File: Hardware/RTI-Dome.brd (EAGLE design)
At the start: 80 x 71.1 mm, 50 parts, among them IC1 24AA128ST, IC2 74LVC244, IC3 FT232RL, IC4 74ABT244, X13 PN61729-S

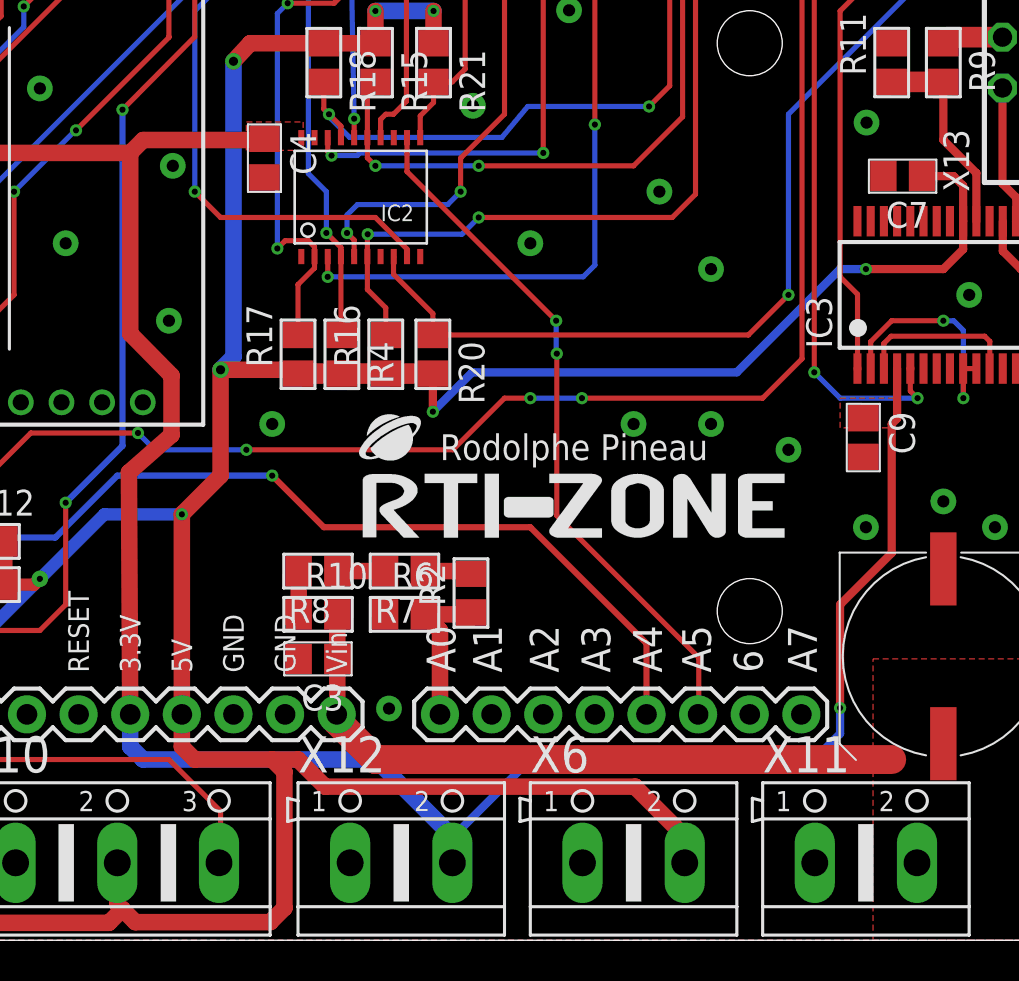
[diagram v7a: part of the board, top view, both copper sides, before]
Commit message: Some routing optimisation. Remove 3.3V header as it's not needed anymore. Added 2 ground for good measure
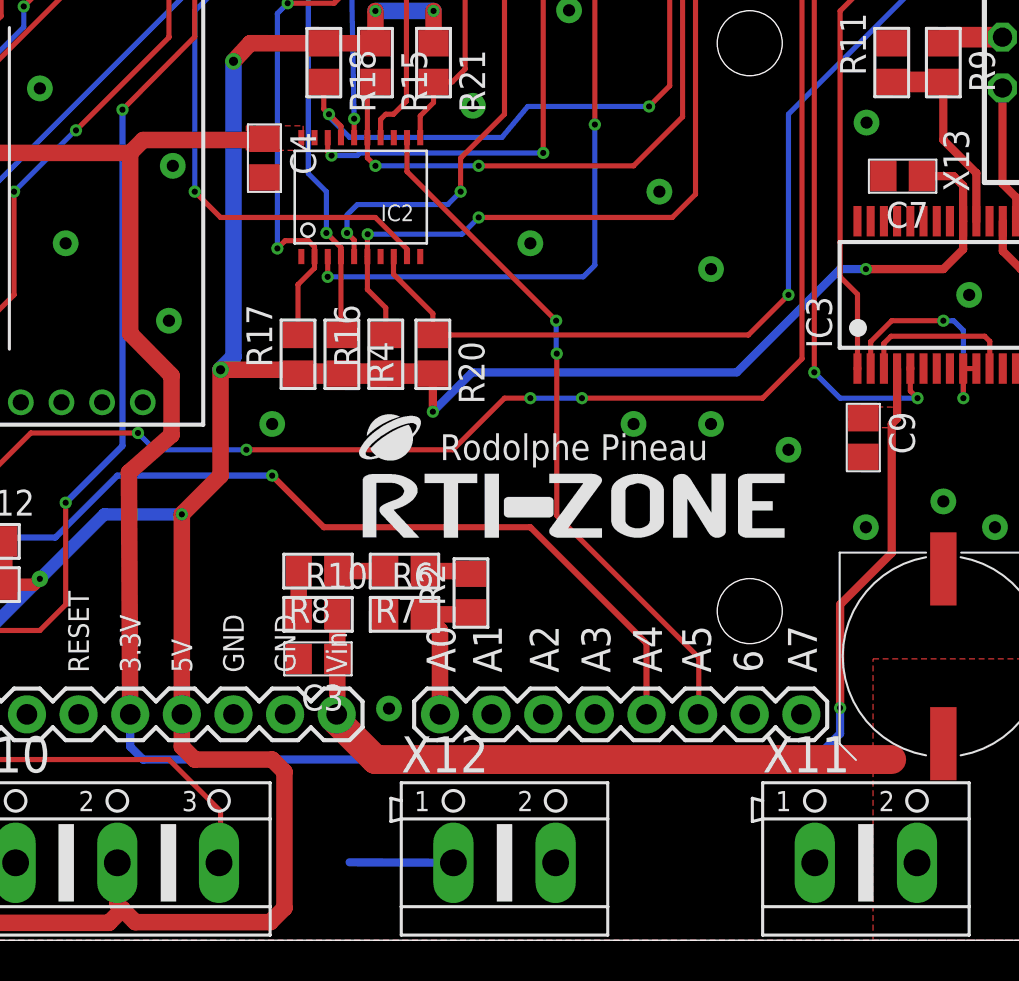
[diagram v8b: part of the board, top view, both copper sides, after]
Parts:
- removed X6: (no value), con-ptr500:AK500/2
- moved X12 5.08 mm to (43.2, 3.81)
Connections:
- net 3.3V: no longer X12.2
- net GND: now also X12.2; no longer X6.1
- net VCC: no longer X6.2
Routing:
- net VCC: track 201.4 -> 178.2 mm
- net GND: track 0.04 -> 5.11 mm
- net 3.3V: track 144.1 -> 139.6 mm
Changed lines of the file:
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@@
 <attribute name="OC_NEWARK" value="34R5507" x="16.383" y="37.465" size="1.778" layer="27" rot="R90" display="off"/>
-</element>
-<element name="X6" library="con-ptr500" package="AK500/2" value="" x="49.53" y="3.81">
-<attribute name="OC_FARNELL" value="unknown" x="49.53" y="3.81" size="1.778" layer="27" display="off"/>
-<attribute name="MF" value="" x="49.53" y="3.81" size="1.778" layer="27" display="off"/>
-<attribute name="MPN" value="" x="49.53" y="3.81" size="1.778" layer="27" display="off"/>
-<attribute name="OC_NEWARK" value="unknown" x="49.53" y="3.81" size="1.778" layer="27" display="off"/>
 </element>
 <element name="PCB1" library="arduino_shield" package="ARDUINO_DUE_SHIELD_SHORT" value="ARDUINO_DUE_SHIELD_SHORT" x="40.005" y="32.7025"/>
@@
 <element name="R3" library="rti" package="R0805" value="1K" x="1.93675" y="44.45" rot="R270"/>
 <element name="C5" library="rti" package="C0805" value="100nF" x="1.93675" y="40.22725" rot="R270"/>
-<element name="X12" library="con-ptr500" package="AK500/2" value="" x="38.1" y="3.81">
-<attribute name="OC_NEWARK" value="unknown" x="38.1" y="3.81" size="1.778" layer="27" display="off"/>
-<attribute name="OC_FARNELL" value="unknown" x="38.1" y="3.81" size="1.778" layer="27" display="off"/>
-<attribute name="MF" value="" x="38.1" y="3.81" size="1.778" layer="27" display="off"/>
-<attribute name="MPN" value="" x="38.1" y="3.81" size="1.778" layer="27" display="off"/>
+<element name="X12" library="con-ptr500" package="AK500/2" value="" x="43.18" y="3.81">
+<attribute name="OC_NEWARK" value="unknown" x="43.18" y="3.81" size="1.778" layer="27" display="off"/>
+<attribute name="OC_FARNELL" value="unknown" x="43.18" y="3.81" size="1.778" layer="27" display="off"/>
+<attribute name="MF" value="" x="43.18" y="3.81" size="1.778" layer="27" display="off"/>
+<attribute name="MPN" value="" x="43.18" y="3.81" size="1.778" layer="27" display="off"/>
 </element>
 <element name="IC3" library="ftdichip" package="SSOP28" value="FT232RL" x="64.77" y="31.75">
@@
 <via x="53.34" y="33.02" extent="1-16" drill="0.6" diameter="1.27"/>
 <contactref element="X12" pad="1"/>
-<wire x1="35.56" y1="3.8354" x2="35.5854" y2="3.81" width="0.4064" layer="16"/>
-<contactref element="X6" pad="1"/>
+<wire x1="35.56" y1="3.8354" x2="40.6654" y2="3.81" width="0.4064" layer="16"/>
 <via x="66.04" y="31.75" extent="1-16" drill="0.6" diameter="1.27"/>
 <contactref element="IC2" pad="P$13"/>
@@
 <contactref element="IC4" pad="P$8"/>
 <contactref element="IC4" pad="P$11"/>
+<contactref element="X12" pad="2"/>
 <wire x1="14.37" y1="16.165" x2="14.37" y2="19.415" width="0" layer="19" extent="1-1"/>
 </signal>
@@
 <wire x1="31.428" y1="39.49" x2="31.369" y2="39.431" width="0.4064" layer="1"/>
 <polygon width="0.254" layer="1" isolate="0.254" thermals="no">
-<vertex x="30.48" y="40.259"/>
-<vertex x="33.274" y="40.259"/>
+<vertex x="30.48" y="40.0685"/>
+<vertex x="33.274" y="40.0685"/>
 <vertex x="33.274" y="38.862"/>
 <vertex x="30.48" y="38.862"/>
@@
 <contactref element="C5" pad="1"/>
 <wire x1="1.93675" y1="43.5" x2="1.93675" y2="41.17725" width="0.6096" layer="1"/>
-<wire x1="24.765" y1="11.1125" x2="24.765" y2="9.525" width="0.8128" layer="16"/>
-<wire x1="24.765" y1="9.525" x2="25.4" y2="8.89" width="0.8128" layer="16"/>
-<wire x1="25.4" y1="8.89" x2="36.8554" y2="8.89" width="0.8128" layer="16"/>
 <contactref element="IC3" pad="4"/>
 <wire x1="62.23" y1="25.4" x2="62.23" y2="19.05" width="0.4064" layer="1"/>
@@
 <contactref element="C9" pad="1"/>
 <polygon width="0.4064" layer="1" thermals="no">
-<vertex x="59.69" y="26.67"/>
-<vertex x="62.51575" y="26.67"/>
+<vertex x="60.10275" y="26.25725"/>
+<vertex x="62.51575" y="26.2255"/>
 <vertex x="62.51575" y="25.2095"/>
-<vertex x="59.69" y="25.2095"/>
+<vertex x="60.10275" y="25.24125"/>
 </polygon>
 <wire x1="62.495" y1="28.125" x2="62.495" y2="25.665" width="0.4064" layer="1"/>
 <wire x1="62.495" y1="25.665" x2="62.23" y2="25.4" width="0.4064" layer="1"/>
-<contactref element="X12" pad="2"/>
-<wire x1="36.8554" y1="8.89" x2="38.1254" y2="7.5946" width="0.8128" layer="16"/>
-<wire x1="38.1254" y1="7.5946" x2="40.64" y2="5.08" width="0.8128" layer="16"/>
-<wire x1="40.64" y1="5.08" x2="40.64" y2="3.8354" width="0.8128" layer="16"/>
-<wire x1="40.64" y1="3.8354" x2="40.6146" y2="3.81" width="0.8128" layer="16"/>
-<wire x1="58.42" y1="8.89" x2="44.45" y2="8.89" width="0.4064" layer="16"/>
-<wire x1="44.45" y1="8.89" x2="40.64" y2="5.08" width="0.4064" layer="16"/>
+<wire x1="58.42" y1="8.89" x2="25.4" y2="8.89" width="0.4064" layer="16"/>
+<wire x1="25.4" y1="8.89" x2="24.765" y2="9.525" width="0.4064" layer="16"/>
+<wire x1="24.765" y1="9.525" x2="24.765" y2="11.1125" width="0.4064" layer="16"/>
 </signal>
 <signal name="RG-11-IN_5V">
@@
 <contactref element="PCB1" pad="5V"/>
 <wire x1="27.305" y1="20.955" x2="29.21" y2="22.86" width="0.8128" layer="1"/>
-<wire x1="34.3535" y1="7.5565" x2="49.6189" y2="7.5565" width="0.8128" layer="1"/>
 <contactref element="IC3" pad="20"/>
 <wire x1="65.745" y1="35.375" x2="65.745" y2="33.995" width="0.4064" layer="1"/>
@@
 <via x="39.6875" y="45.72" extent="1-16" drill="0.3"/>
 <wire x1="39.6875" y1="45.72" x2="39.6875" y2="44.13" width="0.8128" layer="1"/>
-<contactref element="X6" pad="2"/>
-<wire x1="49.6189" y1="7.5565" x2="49.6189" y2="7.5311" width="0.8128" layer="1"/>
-<wire x1="49.6189" y1="7.5311" x2="52.07" y2="5.08" width="0.8128" layer="1"/>
-<wire x1="52.07" y1="5.08" x2="52.07" y2="3.8354" width="0.8128" layer="1"/>
-<wire x1="52.07" y1="3.8354" x2="52.0446" y2="3.81" width="0.8128" layer="1"/>
 <contactref element="X9" pad="3"/>
 <contactref element="X9" pad="1"/>
@@
 <wire x1="27.305" y1="9.525" x2="27.94" y2="8.89" width="0.8128" layer="1"/>
 <wire x1="27.94" y1="8.89" x2="31.75" y2="8.89" width="0.8128" layer="1"/>
-<wire x1="31.75" y1="8.89" x2="33.02" y2="8.89" width="0.8128" layer="1"/>
-<wire x1="33.02" y1="8.89" x2="34.3535" y2="7.5565" width="0.8128" layer="1"/>
 <wire x1="32.35325" y1="1.5875" x2="32.35325" y2="8.28675" width="0.8128" layer="1"/>
 <wire x1="32.35325" y1="8.28675" x2="31.75" y2="8.89" width="0.8128" layer="1"/>
